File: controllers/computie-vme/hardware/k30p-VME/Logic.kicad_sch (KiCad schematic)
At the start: 9 parts, among them J3 JTAG, U17 74LS30, U3 74HC05, U4 ATF1508AS-xxAx100

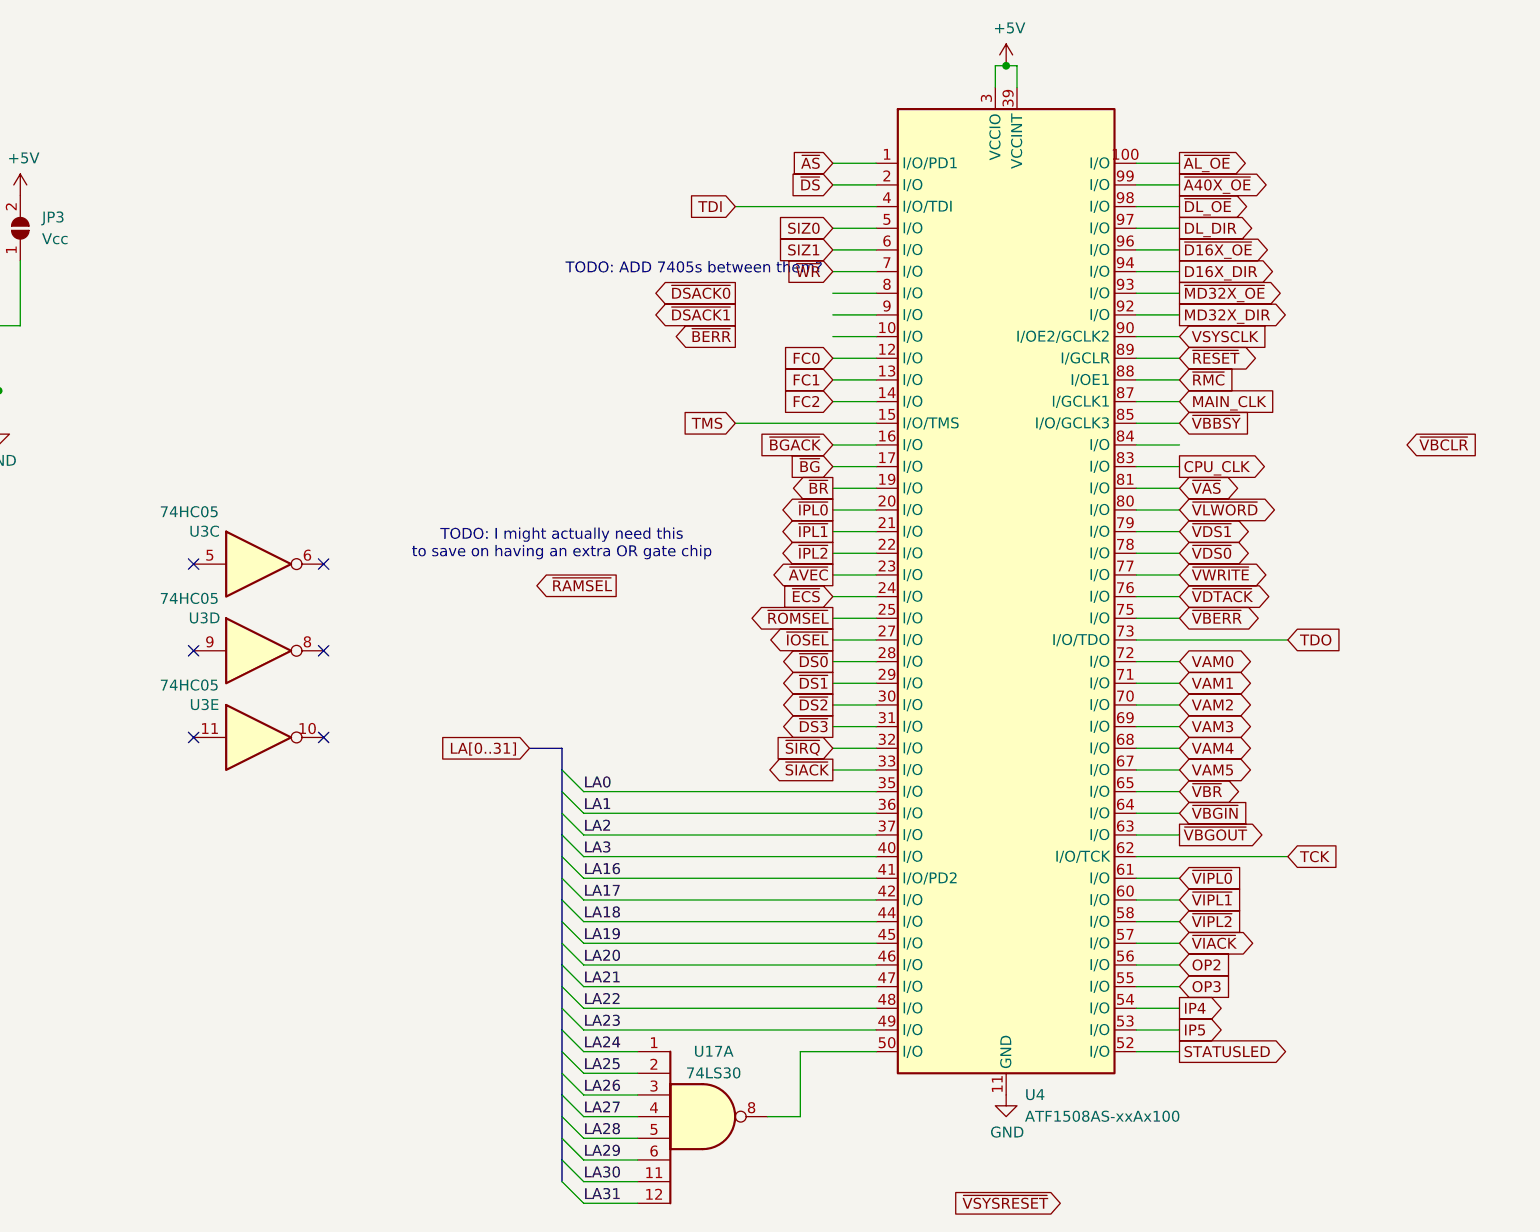
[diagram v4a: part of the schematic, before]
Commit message: Schematics for k30p-VME more or less done
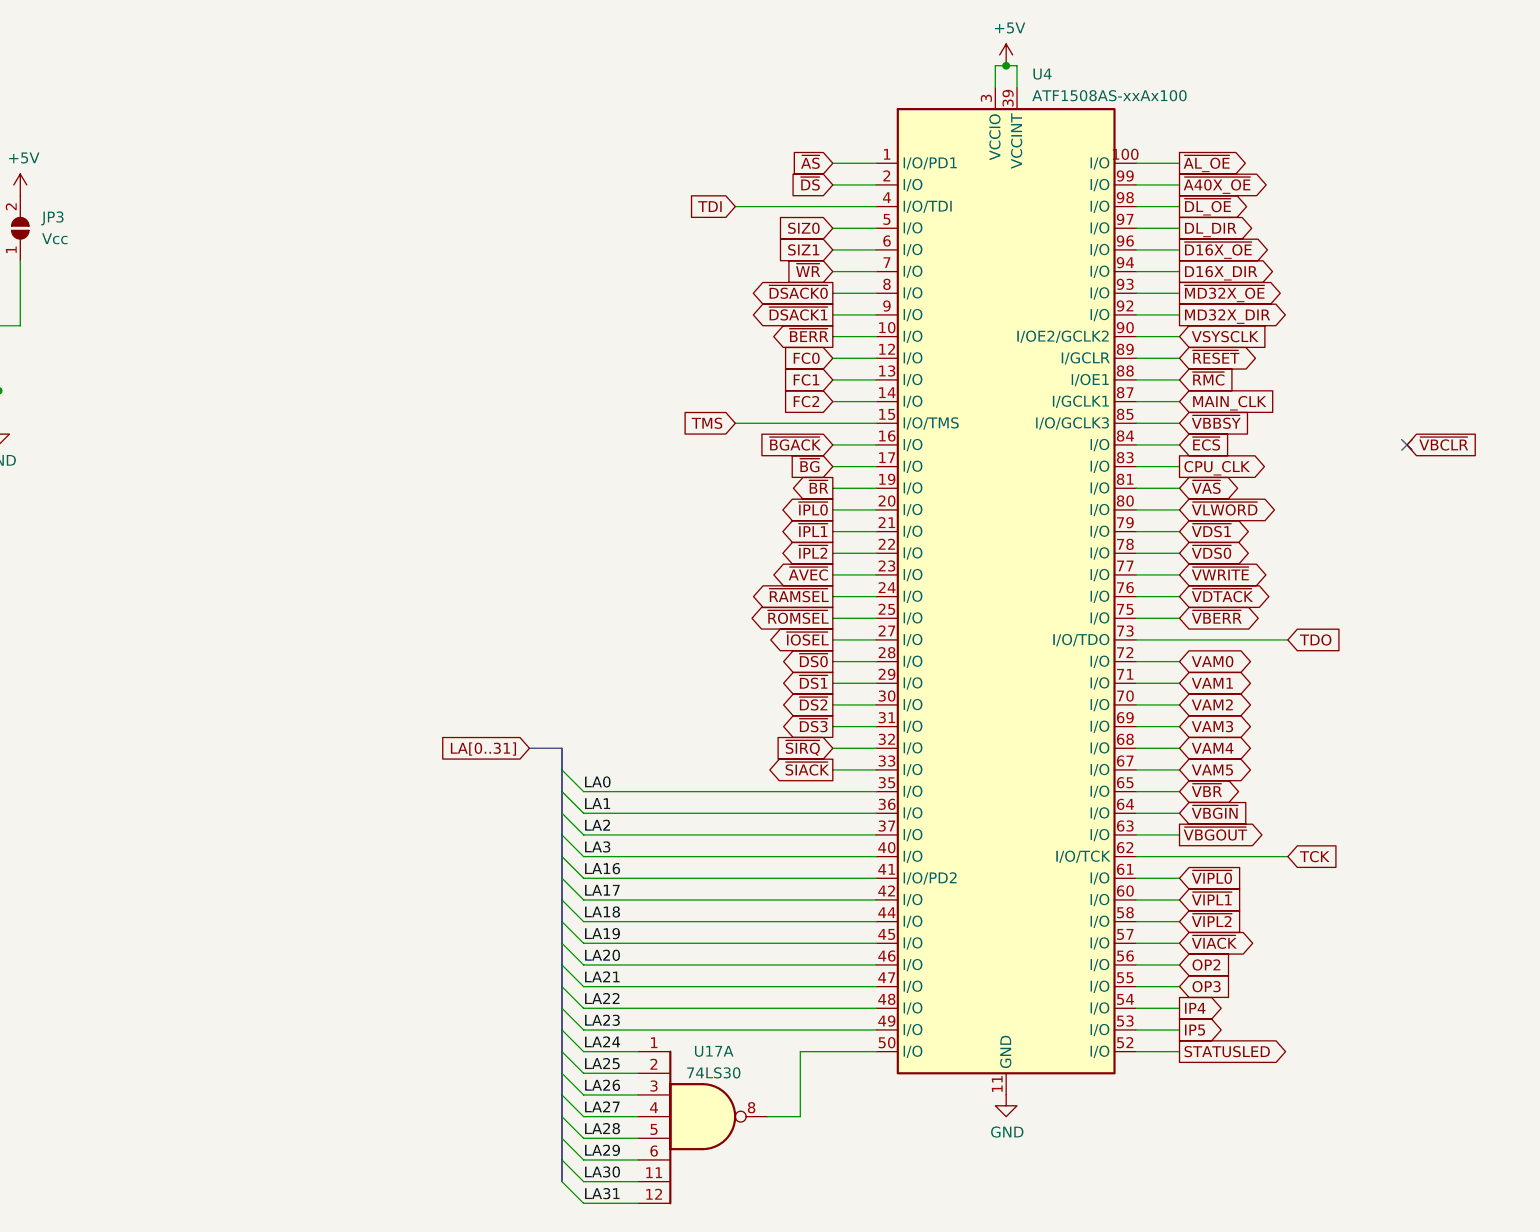
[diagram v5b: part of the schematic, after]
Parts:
- removed U3: 74HC05, Package_SO:TSSOP-14_4.4x5mm_P0.65mm, symbol 74xx:74LS05
- U17: footprint (none) -> Package_SO:TSSOP-14_4.4x5mm_P0.65mm
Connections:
- net ~{BERR}: now also U4.10 (I/O)
- net ~{DSACK0}: now also U4.8 (I/O)
- net ~{DSACK1}: now also U4.9 (I/O)
- net ~{ECS}: now also U4.84 (I/O); no longer U4.24 (I/O)
- net ~{RAMSEL}: now also U4.24 (I/O)
- no-connect marks 9 -> 4
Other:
- note removed: "TODO: ADD 7405s between them?"
- note removed: "TODO: I might actually need this to save on having an extra OR gate chip"

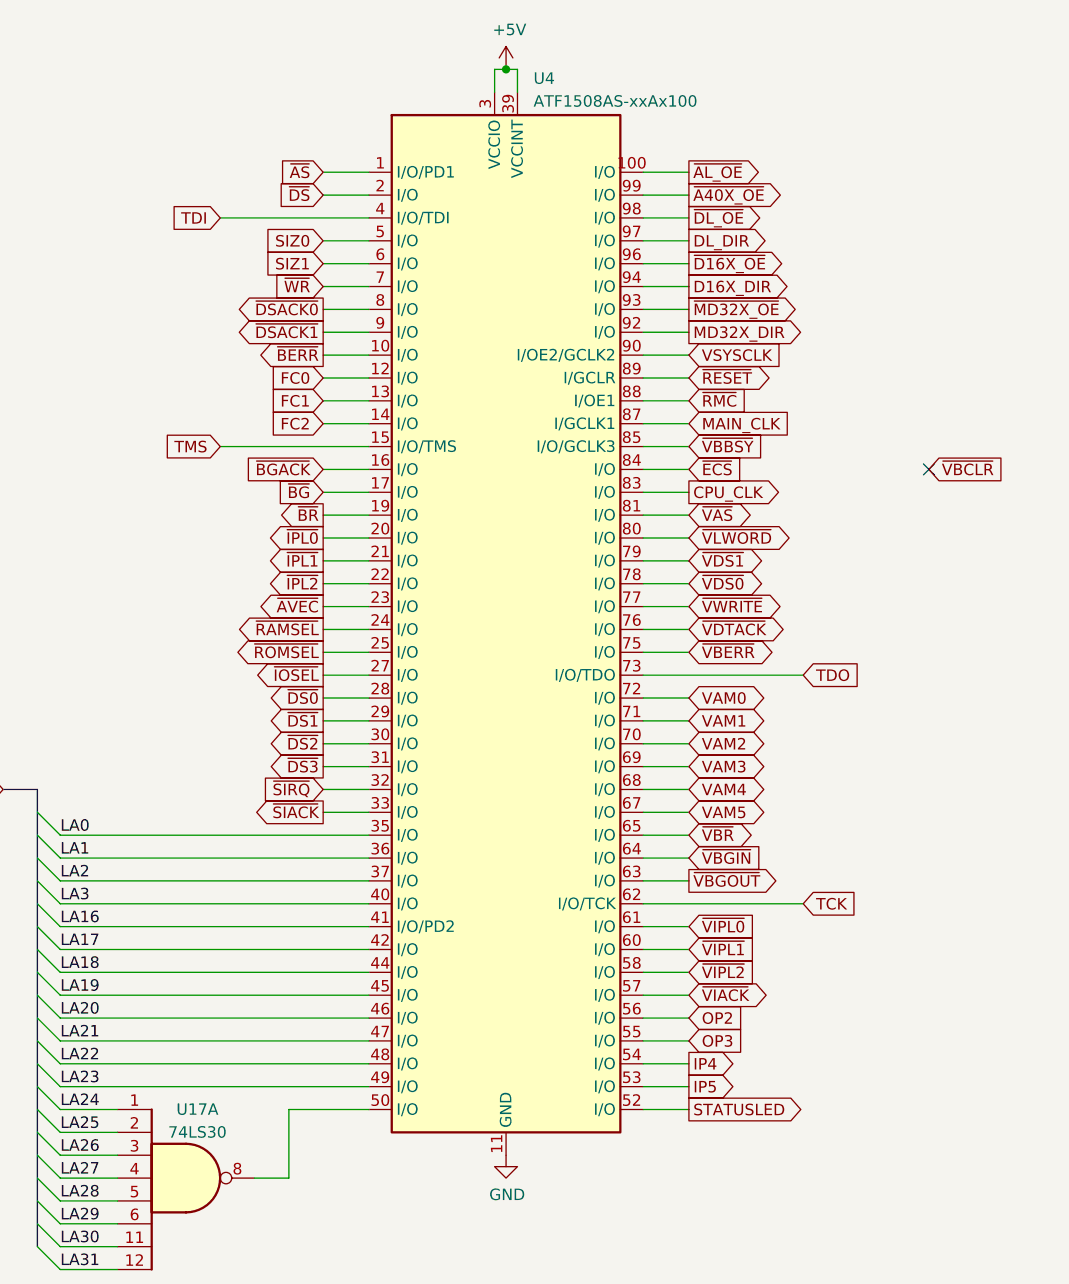
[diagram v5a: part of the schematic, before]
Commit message: Mostly finished k30p-VME board and frontpanel
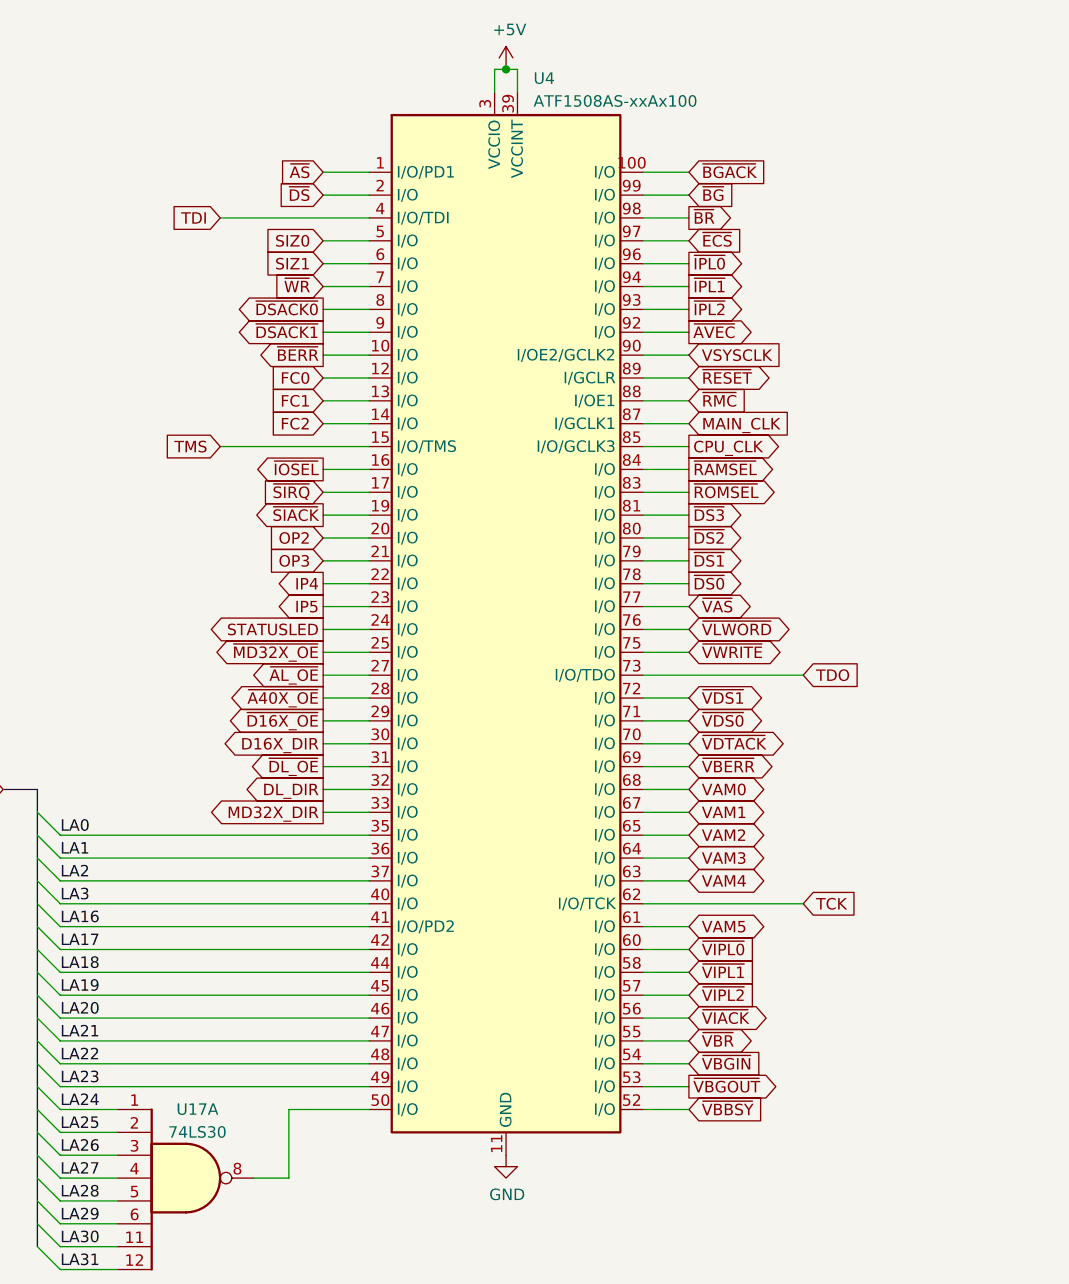
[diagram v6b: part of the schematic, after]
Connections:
- net CPU_CLK: now also U4.85 (I/O/GCLK3); no longer U4.83 (I/O)
- net D16X_DIR: now also U4.30 (I/O); no longer U4.94 (I/O)
- net DL_DIR: now also U4.32 (I/O); no longer U4.97 (I/O)
- net IP4: now also U4.22 (I/O); no longer U4.54 (I/O)
- net IP5: now also U4.23 (I/O); no longer U4.53 (I/O)
- net MD32X_DIR: now also U4.33 (I/O); no longer U4.92 (I/O)
- net OP2: now also U4.20 (I/O); no longer U4.56 (I/O)
- net OP3: now also U4.21 (I/O); no longer U4.55 (I/O)
- net STATUSLED: now also U4.24 (I/O); no longer U4.52 (I/O)
- net VAM0: now also U4.68 (I/O); no longer U4.72 (I/O)
- net VAM1: now also U4.67 (I/O); no longer U4.71 (I/O)
- net VAM2: now also U4.65 (I/O); no longer U4.70 (I/O)
- net VAM3: now also U4.64 (I/O); no longer U4.69 (I/O)
- net VAM4: now also U4.63 (I/O); no longer U4.68 (I/O)
- net VAM5: now also U4.61 (I/O); no longer U4.67 (I/O)
- net ~{A40X_OE}: now also U4.28 (I/O); no longer U4.99 (I/O)
- net ~{AL_OE}: now also U4.27 (I/O); no longer U4.100 (I/O)
- net ~{AVEC}: now also U4.92 (I/O); no longer U4.23 (I/O)
- net ~{BGACK}: now also U4.100 (I/O); no longer U4.16 (I/O)
- net ~{BG}: now also U4.99 (I/O); no longer U4.17 (I/O)
- net ~{BR}: now also U4.98 (I/O); no longer U4.19 (I/O)
- net ~{D16X_OE}: now also U4.29 (I/O); no longer U4.96 (I/O)
- net ~{DL_OE}: now also U4.31 (I/O); no longer U4.98 (I/O)
- net ~{DS0}: now also U4.78 (I/O); no longer U4.28 (I/O)
- net ~{DS1}: now also U4.79 (I/O); no longer U4.29 (I/O)
- net ~{DS2}: now also U4.80 (I/O); no longer U4.30 (I/O)
- net ~{DS3}: now also U4.81 (I/O); no longer U4.31 (I/O)
- net ~{ECS}: now also U4.97 (I/O); no longer U4.84 (I/O)
- net ~{IOSEL}: now also U4.16 (I/O); no longer U4.27 (I/O)
- net ~{IPL0}: now also U4.96 (I/O); no longer U4.20 (I/O)
- net ~{IPL1}: now also U4.94 (I/O); no longer U4.21 (I/O)
- net ~{IPL2}: now also U4.93 (I/O); no longer U4.22 (I/O)
- net ~{MD32X_OE}: now also U4.25 (I/O); no longer U4.93 (I/O)
- net ~{RAMSEL}: now also U4.84 (I/O); no longer U4.24 (I/O)
- net ~{ROMSEL}: now also U4.83 (I/O); no longer U4.25 (I/O)
- net ~{SIACK}: now also U4.19 (I/O); no longer U4.33 (I/O)
- net ~{SIRQ}: now also U4.17 (I/O); no longer U4.32 (I/O)
- net ~{VAS}: now also U4.77 (I/O); no longer U4.81 (I/O)
- net ~{VBBSY}: now also U4.52 (I/O); no longer U4.85 (I/O/GCLK3)
- net ~{VBERR}: now also U4.69 (I/O); no longer U4.75 (I/O)
- net ~{VBGIN}: now also U4.54 (I/O); no longer U4.64 (I/O)
- net ~{VBGOUT}: now also U4.53 (I/O); no longer U4.63 (I/O)
- net ~{VBR}: now also U4.55 (I/O); no longer U4.65 (I/O)
- net ~{VDS0}: now also U4.71 (I/O); no longer U4.78 (I/O)
- net ~{VDS1}: now also U4.72 (I/O); no longer U4.79 (I/O)
- net ~{VDTACK}: now also U4.70 (I/O); no longer U4.76 (I/O)
- net ~{VIACK}: now also U4.56 (I/O); no longer U4.57 (I/O)
- net ~{VIPL0}: now also U4.60 (I/O); no longer U4.61 (I/O)
- net ~{VIPL1}: now also U4.58 (I/O); no longer U4.60 (I/O)
- net ~{VIPL2}: now also U4.57 (I/O); no longer U4.58 (I/O)
- net ~{VLWORD}: now also U4.76 (I/O); no longer U4.80 (I/O)
- net ~{VWRITE}: now also U4.75 (I/O); no longer U4.77 (I/O)
- no-connect marks 4 -> 3

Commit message: Added MemBird - Woodcock (16-bit VME memory card)
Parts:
- U17: value 74LS30 -> 74HC30
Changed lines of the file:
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@@
 			)
 		)
-		(property "Value" "74LS30"
+		(property "Value" "74HC30"
 			(at 152.4 144.78 0)
 			(effects
